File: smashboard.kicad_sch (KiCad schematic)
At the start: 78 parts, among them J1 OLED, U1 Nice_Nano_V2

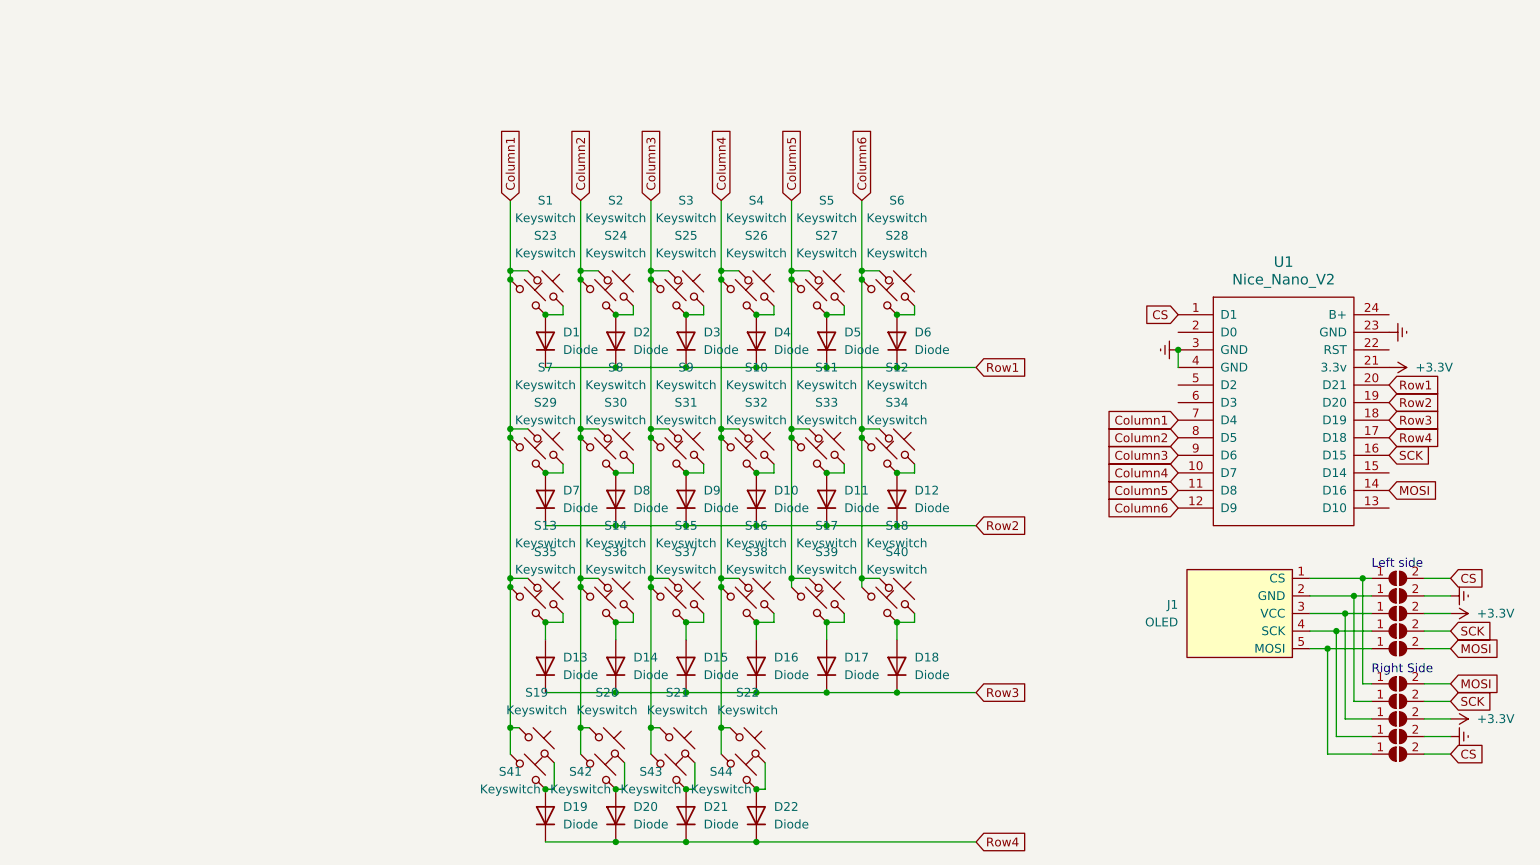
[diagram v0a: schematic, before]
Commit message: PCB: Reset button, on/off button and some modification in the vias
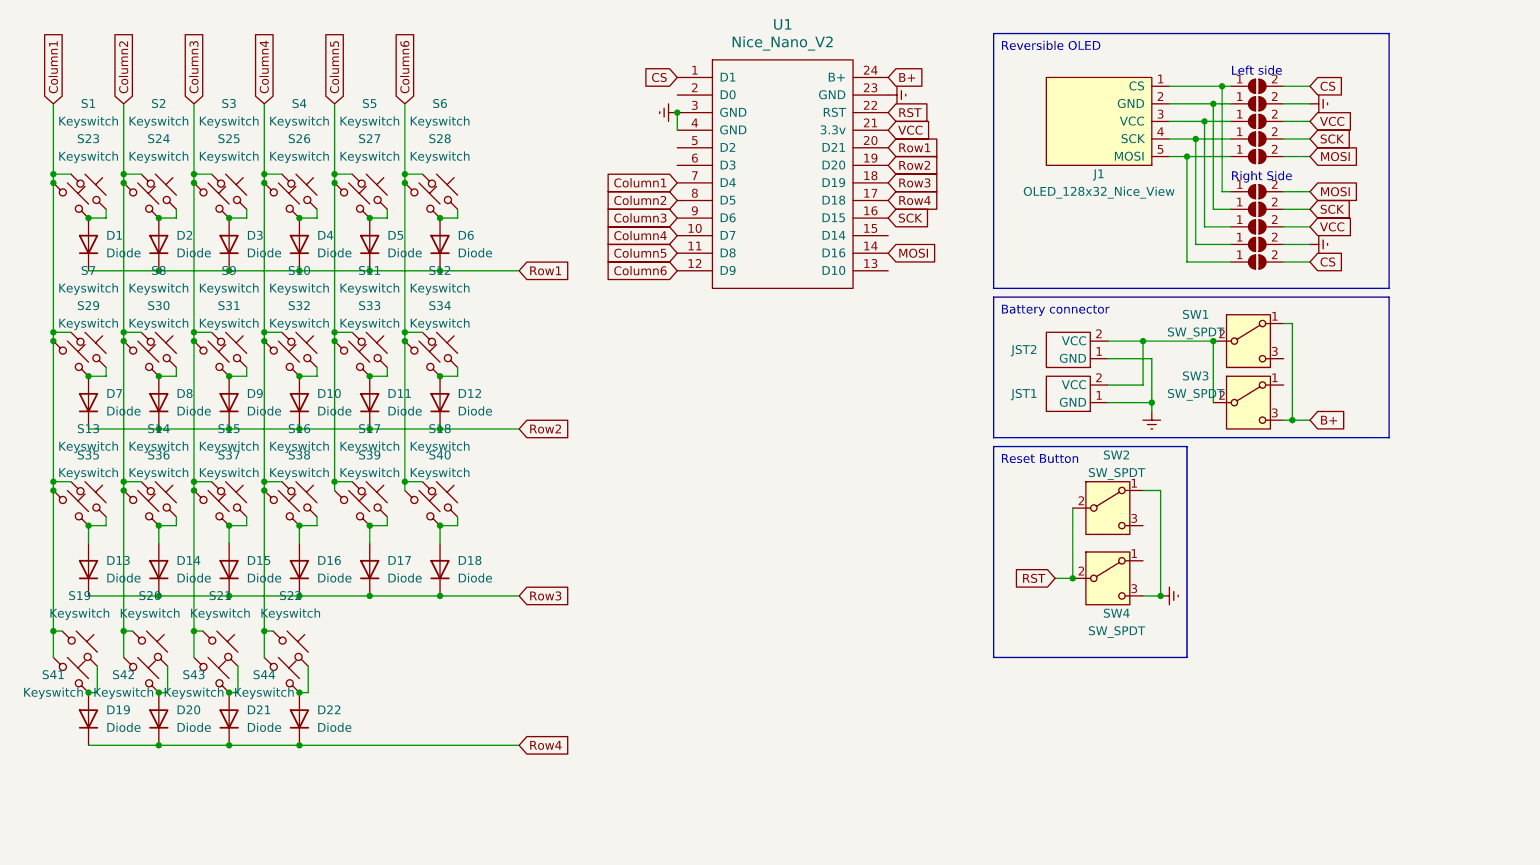
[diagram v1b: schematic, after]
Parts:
- added JST1, JST2: ~, Connector_JST:JST_PH_S2B-PH-K_1x02_P2.00mm_Horizontal, symbol ScottoKeebs:Battery_Connector
- added SW1, SW2, SW3, SW4: SW_SPDT, Button_Switch_SMD:SW_SPDT_PCM12, symbol Switch:SW_SPDT
- J1: value OLED -> OLED_128x32_Nice_View
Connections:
- net Earth: now also JST1.1 (GND), JST2.1 (GND), SW2.1 (A), SW4.3 (C)
- net RST: now reaches U1.22 (RST)
- net RST: now also SW2.2 (B), SW4.2 (B)
- net B+: now reaches U1.24 (B+)
- net B+: now also SW1.1 (A), SW3.3 (C)
- net +3.3V renamed VCC
- new net: JST1.2 (VCC), JST2.2 (VCC), SW1.2 (B), SW3.2 (B)
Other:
- moved on the sheet: D1, D10, D11, D12, D13, D14, D15, D16, D17, D18, D19, D2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

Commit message: Modified reset and on/off buttons footprints
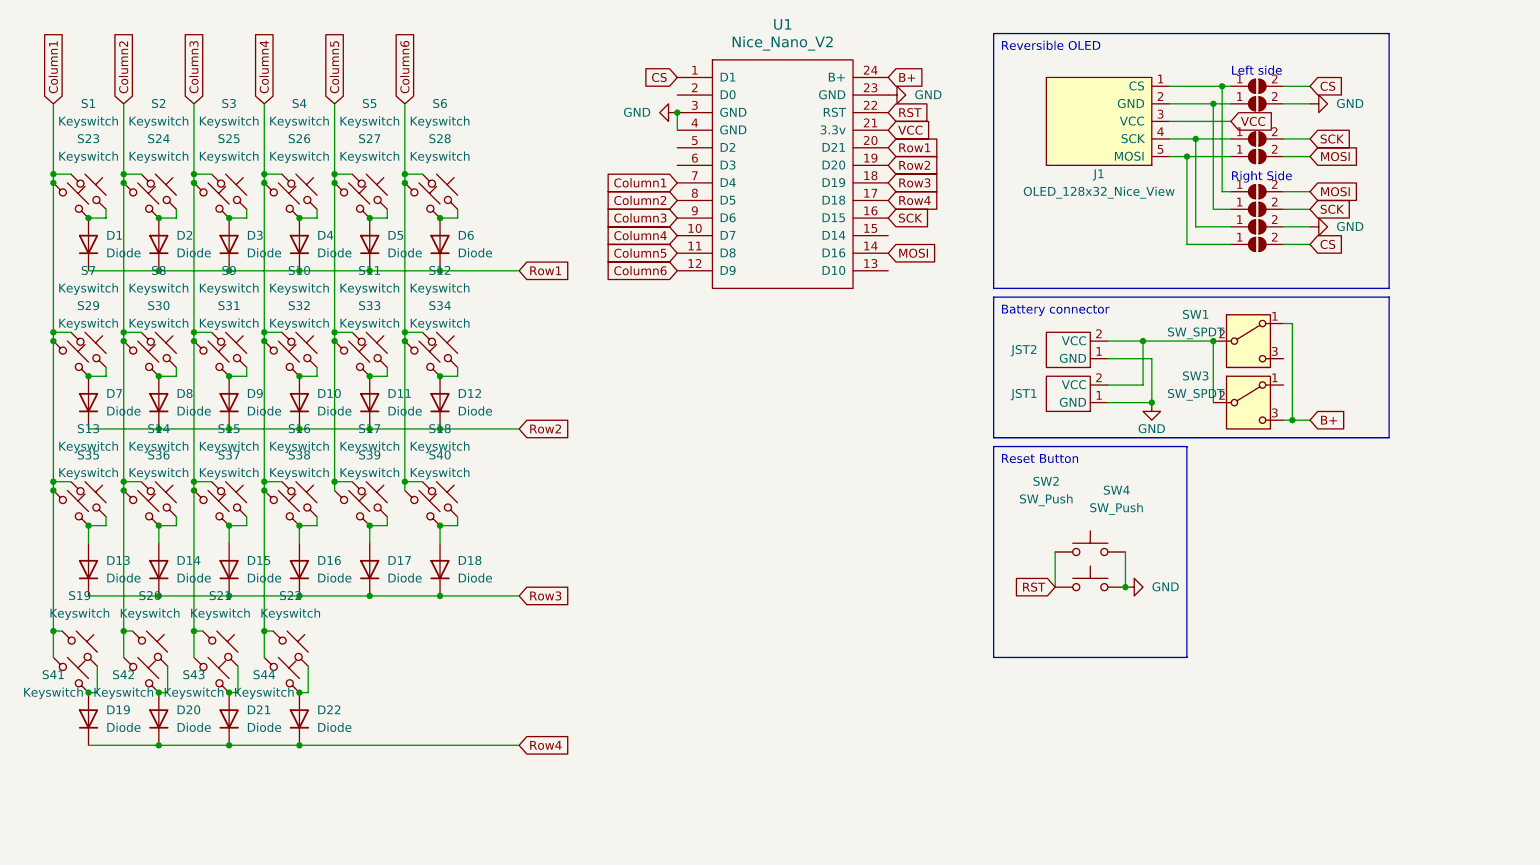
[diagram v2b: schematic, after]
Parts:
- removed JP3, JP8: SolderJumper_2_Open, Jumper:SolderJumper-2_P1.3mm_Open_TrianglePad1.0x1.5mm, symbol Jumper:SolderJumper_2_Open
- removed SW2, SW4: SW_SPDT, Button_Switch_SMD:SW_SPDT_PCM12, symbol Switch:SW_SPDT
- added SW2, SW4: SW_Push, Button_Switch_SMD:Panasonic_EVQPUK_EVQPUB, symbol Switch:SW_Push
- S1, S10, S11, S12, S13, S14, S15, S16, S17, S18, S2, S23, S24, S25, S26, S27, S28, S29, S3, S30, S31, S32, S33, S34, S35, S36, S37, S38, S39, S4, S40, S5, S6, S7, S8, S9: footprint ScottoKeebs_Hotswap:Hotswap_Choc_V1V2_1.00u -> ScottoKeebs_Hotswap:Hotswap_Choc_V1V2
- S19, S20, S21, S41, S42, S43: footprint ScottoKeebs_Hotswap:Hotswap_Choc_V1V2_1.25u -> ScottoKeebs_Hotswap:Hotswap_Choc_V1V2
- S22, S44: footprint ScottoKeebs_Hotswap:Hotswap_Choc_V1V2_2.25u -> ScottoKeebs_Hotswap:Hotswap_Choc_V1V2
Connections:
- net RST: now also SW2.1, SW4.1
- net VCC: now also J1.3 (VCC)
- net Earth renamed GND
- net GND: now also SW2.2, SW4.2
